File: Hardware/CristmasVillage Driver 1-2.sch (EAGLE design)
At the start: 54 parts, among them CN1 MJ-180SMT, CN2-PROG JST-6PSPI-SIDE-S6B, CN3-SERIAL JST-4PSIDE-S4B, CN5-LEDSTRIPS HDR_2X10_SIDE-MOUNT, IC1 UA78M05DCY, IC2 LM358D, IC3 LM358D, IC4 LM358D, IC5 ATTINY-4/5/9/10, IC6 TINY2313-*S*, Q1 Si2309CD, Q10 NX7002AKW, Q11 NX7002AKW, Q12 NX7002AKW, Q2 NX7002AKW, Q3 NX7002AKW, Q4 NX7002AKW, Q5 NX7002AKW, Q6 NX7002AKW, Q7 NX7002AKW, Q8 NX7002AKW, Q9 NX7002AKW, SW1 POWER, SW2 NIGHT-MODE

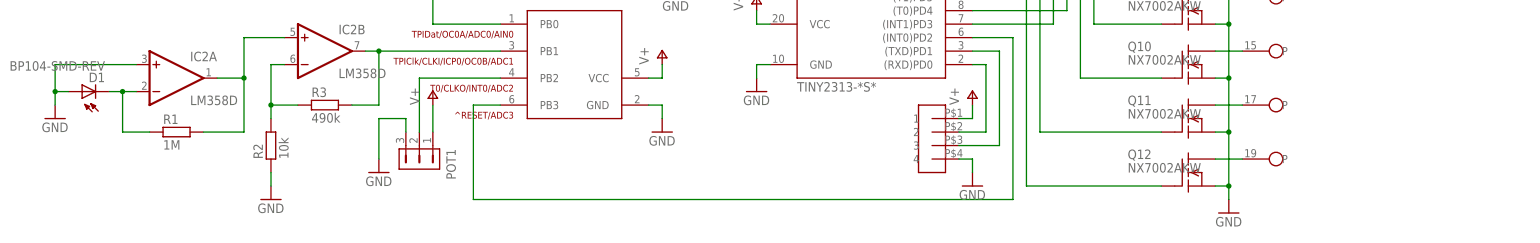
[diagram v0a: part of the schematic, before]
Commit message: Added opt. filter caps to hardware & created PDF exports of v1.2
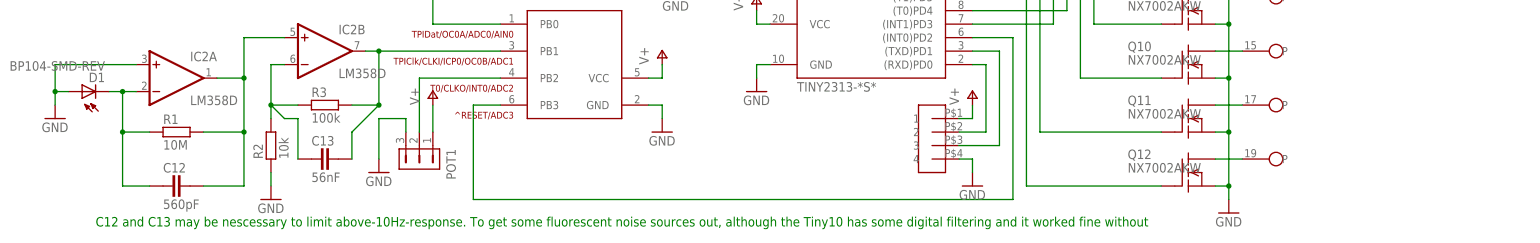
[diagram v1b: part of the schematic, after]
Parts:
- added C12: 560pF, ipc-7351-capacitor:CAPACITOR_0603
- added C13: 56nF, ipc-7351-capacitor:CAPACITOR_0603
- R1: value 1M -> 10M
- R3: value 490k -> 100k
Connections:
- net N$2: now also C12.1
- net N$3: now also C12.2
- net N$6: now also C13.1
- net N$7: now also C13.2
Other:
- note added: "C12 and C13 may be nescessary to limit above-10Hz-response. To get some fluorescent noise sources out, although the Tiny10 has some digital filtering and it worked fine without"
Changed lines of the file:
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@@
 <part name="GND3" library="supply1" deviceset="GND" device=""/>
 <part name="C3" library="ipc-7351-capacitor" deviceset="CAPACITOR_" device="0603" value="100n"/>
-<part name="R1" library="ipc-7351-resistor" deviceset="RESISTOR_" device="0603" value="1M"/>
+<part name="R1" library="ipc-7351-resistor" deviceset="RESISTOR_" device="0603" value="10M"/>
 <part name="Q1" library="ipc-7351-transistor" deviceset="MOSFET-PCH_" device="SOT-23" value="Si2309CD"/>
 <part name="R2" library="ipc-7351-resistor" deviceset="RESISTOR_" device="0603" value="10k"/>
-<part name="R3" library="ipc-7351-resistor" deviceset="RESISTOR_" device="0603" value="490k"/>
+<part name="R3" library="ipc-7351-resistor" deviceset="RESISTOR_" device="0603" value="100k"/>
 <part name="GND4" library="supply1" deviceset="GND" device=""/>
 <part name="IC5" library="avr-6" deviceset="ATTINY-4/5/9/10" device=""/>
@@
 <part name="R12" library="ipc-7351-resistor" deviceset="RESISTOR_" device="0603" value="1M"/>
 <part name="GND15" library="supply1" deviceset="GND" device=""/>
+<part name="C12" library="ipc-7351-capacitor" deviceset="CAPACITOR_" device="0603" value="560pF"/>
+<part name="C13" library="ipc-7351-capacitor" deviceset="CAPACITOR_" device="0603" value="56nF"/>
 </parts>
 <sheets>
 <sheet>
 <plain>
+<text x="30.48" y="2.54" size="1.778" layer="91">C12 and C13 may be nescessary to limit above-10Hz-response. To get some fluorescent noise sources out, although the Tiny10 has some digital filtering and it worked fine without</text>
 </plain>
 <instances>
@@
 <instance part="R12" gate="G$1" x="114.3" y="111.76"/>
 <instance part="GND15" gate="1" x="132.08" y="106.68"/>
+<instance part="C12" gate="G$1" x="45.72" y="10.16"/>
+<instance part="C13" gate="G$1" x="73.66" y="15.24"/>
 </instances>
 <busses>
@@
 <wire x1="35.56" y1="27.94" x2="33.02" y2="27.94" width="0.1524" layer="91"/>
 <junction x="35.56" y="27.94"/>
+<pinref part="C12" gate="G$1" pin="1"/>
+<wire x1="40.64" y1="10.16" x2="35.56" y2="10.16" width="0.1524" layer="91"/>
+<wire x1="35.56" y1="10.16" x2="35.56" y2="20.32" width="0.1524" layer="91"/>
+<junction x="35.56" y="20.32"/>
 </segment>
 </net>
@@
 <wire x1="58.42" y1="38.1" x2="58.42" y2="30.48" width="0.1524" layer="91"/>
 <junction x="58.42" y="30.48"/>
+<pinref part="C12" gate="G$1" pin="2"/>
+<wire x1="50.8" y1="10.16" x2="58.42" y2="10.16" width="0.1524" layer="91"/>
+<wire x1="58.42" y1="10.16" x2="58.42" y2="20.32" width="0.1524" layer="91"/>
+<junction x="58.42" y="20.32"/>
 </segment>
 </net>
@@
 <wire x1="68.58" y1="25.4" x2="63.5" y2="25.4" width="0.1524" layer="91"/>
 <junction x="63.5" y="25.4"/>
+<pinref part="C13" gate="G$1" pin="1"/>
+<wire x1="68.58" y1="15.24" x2="68.58" y2="22.86" width="0.1524" layer="91"/>
+<wire x1="68.58" y1="22.86" x2="66.04" y2="22.86" width="0.1524" layer="91"/>
+<wire x1="66.04" y1="22.86" x2="63.5" y2="25.4" width="0.1524" layer="91"/>
 </segment>
 </net>
@@
 <wire x1="83.82" y1="35.56" x2="106.68" y2="35.56" width="0.1524" layer="91"/>
 <junction x="83.82" y="35.56"/>
-</segment>
-</net>
+<pinref part="C13" gate="G$1" pin="2"/>
+<wire x1="78.74" y1="15.24" x2="78.74" y2="20.32" width="0.1524" layer="91"/>
+<wire x1="78.74" y1="20.32" x2="83.82" y2="25.4" width="0.1524" layer="91"/>
+<junction x="83.82" y="25.4"/>
+</segment>
+</net>
